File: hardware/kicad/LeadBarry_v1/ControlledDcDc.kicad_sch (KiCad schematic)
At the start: 8 parts, among them Q13 AO3420, U4 XL6019E1 Module

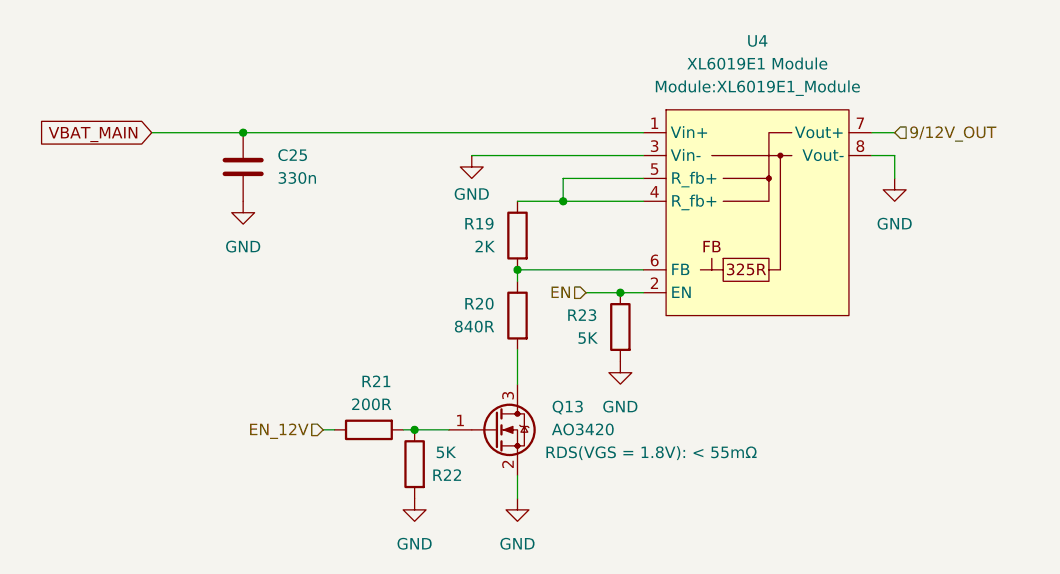
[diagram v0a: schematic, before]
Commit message: fix: PoE sockets and DC output status leds were added
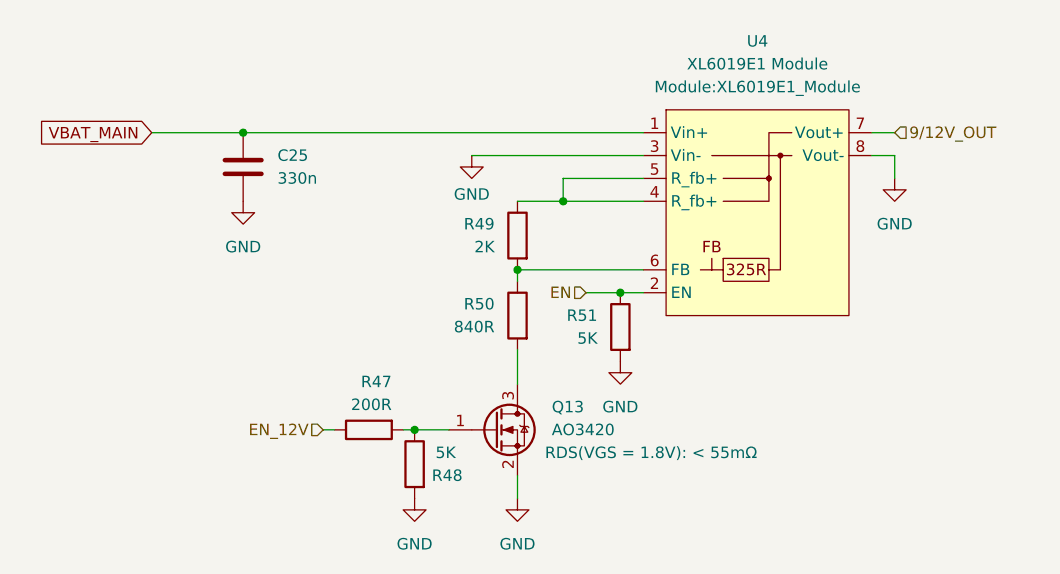
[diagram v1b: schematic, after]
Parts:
- renumbered R21 to R47, R22 to R48, R19 to R49, R20 to R50, R23 to R51
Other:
- title: (none) -> Controlled 9/12V DC/DC Converter Block
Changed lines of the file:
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@@
 	(generator_version "8.0")
 	(paper "A4")
+	(title_block
+		(title "Controlled 9/12V DC/DC Converter Block")
+		(date "2026-03-21")
+	)
 	(junction
 		(at 121.92 118.11)
@@
 		(on_board yes)
 		(dnp no)
-		(property "Reference" "R20"
+		(property "Reference" "R50"
 			(at 130.81 104.1399 0)
 			(effects
@@
 		(on_board yes)
 		(dnp no)
-		(property "Reference" "R23"
+		(property "Reference" "R51"
 			(at 142.24 105.4099 0)
 			(effects
@@
 		(on_board yes)
 		(dnp no)
-		(property "Reference" "R19"
+		(property "Reference" "R49"
 			(at 130.81 95.2499 0)
 			(effects
@@
 		(dnp no)
 		(fields_autoplaced yes)
-		(property "Reference" "#PWR022"
+		(property "Reference" "#PWR051"
 			(at 121.92 132.08 0)
 			(effects
@@
 		(dnp no)
 		(fields_autoplaced yes)
-		(property "Reference" "U?"
+		(property "Reference" "U4"
 			(at 160.02 74.93 0)
 			(effects
@@
 		(on_board yes)
 		(dnp no)
-		(property "Reference" "R22"
+		(property "Reference" "R48"
 			(at 127.254 123.19 0)
 			(effects
@@
 		(dnp no)
 		(fields_autoplaced yes)
-		(property "Reference" "#PWR020"
+		(property "Reference" "#PWR053"
 			(at 133.35 132.08 0)
 			(effects
@@
 		(on_board yes)
 		(dnp no)
-		(property "Reference" "#PWR?"
+		(property "Reference" "#PWR052"
 			(at 128.27 93.98 0)
 			(effects
@@
 					(unit 1)
 				)
+				(path "/20771d85-0a47-48d4-b39f-5d01020408af/1a5c9110-8742-4ce5-925b-2759184d3a24/eebf9a5b-85c1-451b-802d-a0649c09e85e"
+					(reference "C?")
+					(unit 1)
+				)
 			)
 		)
@@
 		(on_board yes)
 		(dnp no)
-		(property "Reference" "R21"
+		(property "Reference" "R47"
 			(at 119.38 112.776 90)
 			(effects
@@
 		(dnp no)
 		(fields_autoplaced yes)
-		(property "Reference" "#PWR023"
+		(property "Reference" "#PWR054"
 			(at 144.78 116.84 0)
 			(effects
@@
 		(dnp no)
 		(fields_autoplaced yes)
-		(property "Reference" "#PWR046"
+		(property "Reference" "#PWR050"
 			(at 102.87 99.06 0)
 			(effects
@@
 		(dnp no)
 		(fields_autoplaced yes)
-		(property "Reference" "#PWR021"
+		(property "Reference" "#PWR055"
 			(at 175.26 96.52 0)
 			(effects
@@
 					(unit 1)
 				)
+				(path "/20771d85-0a47-48d4-b39f-5d01020408af/1a5c9110-8742-4ce5-925b-2759184d3a24/eebf9a5b-85c1-451b-802d-a0649c09e85e"
+					(reference "Q?")
+					(unit 1)
+				)

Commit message: fix: added display and timer to the schematic
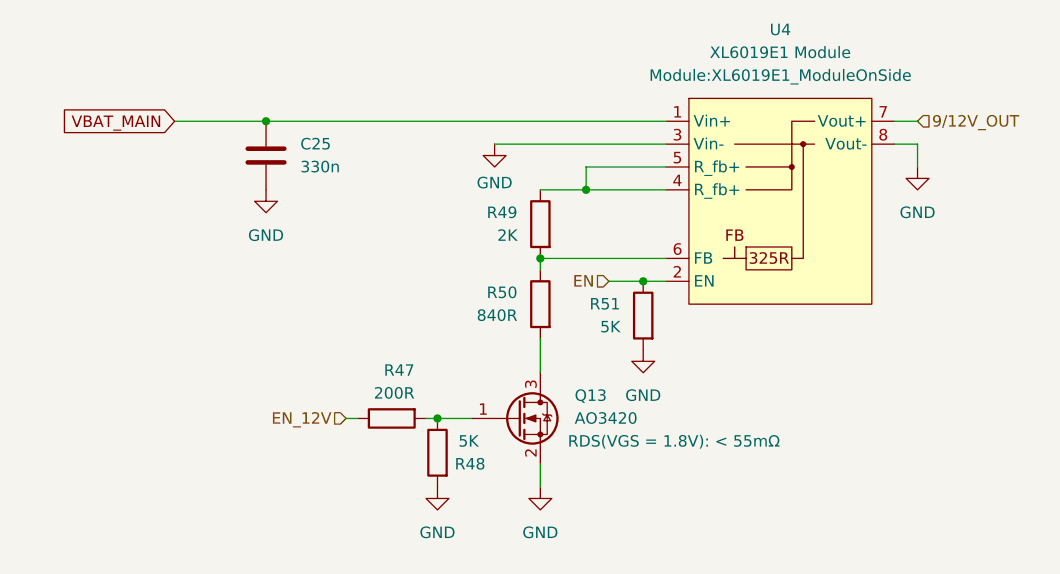
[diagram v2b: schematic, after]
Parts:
- U4: footprint Module:XL6019E1_Module -> Module:XL6019E1_ModuleOnSide
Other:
- moved on the sheet: C25, Q13, R47, R48, R49, R50, R51, U4
